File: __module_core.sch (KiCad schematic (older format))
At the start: 68 parts, among them J1 Vref, J2 bus_L, J3 tri, J4 bus_R, J5 power_bus, U1 TL074, U2 L78L05_TO92, U3 L79L05_TO92, U4 SSI2131, U5 LM317L_TO92

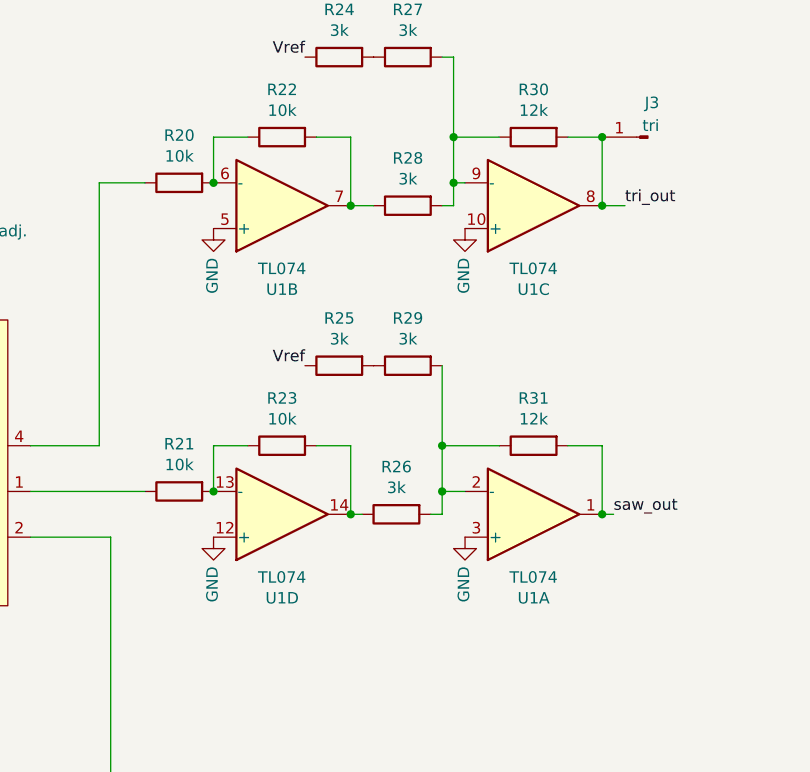
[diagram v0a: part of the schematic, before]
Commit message: Artworks on pcbs are done.
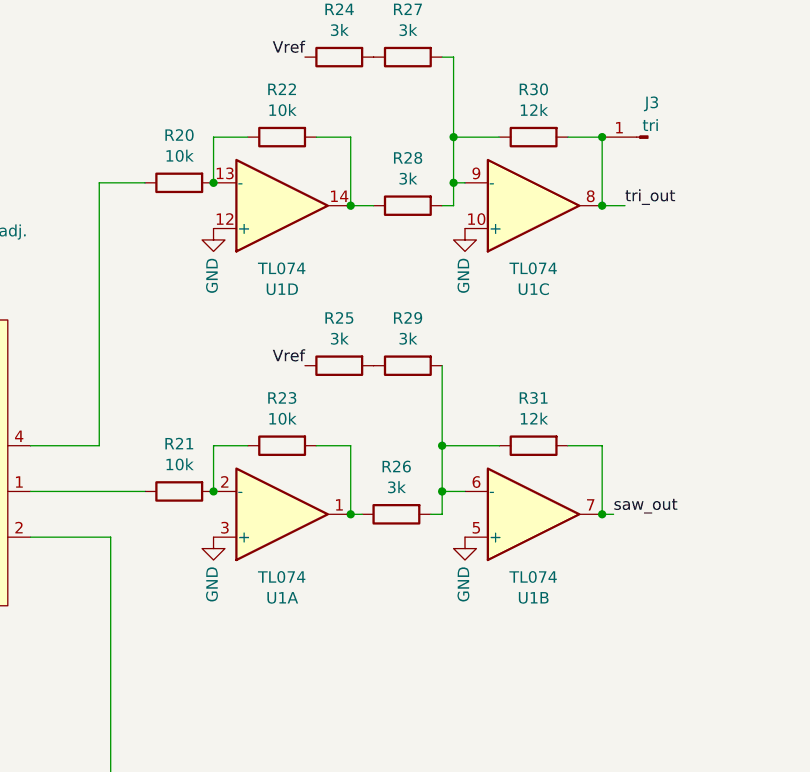
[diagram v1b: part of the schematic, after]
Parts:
- C14, C16, C18: footprint Capacitor_THT:CP_Radial_D5.0mm_P2.50mm -> Capacitor_THT:CP_Radial_Tantal_D5.0mm_P2.50mm
- C7: footprint Capacitor_THT:C_Radial_D10.0mm_H12.5mm_P5.00mm -> Attenuverter:C_Axial_L4.8mm_D3.1mm_P5.08mm_Horizontal
- D3: footprint Diode_THT:D_DO-35_SOD27_P7.62mm_Horizontal -> Diode_THT:D_DO-35_SOD27_P2.54mm_Vertical_AnodeUp
- U2, U3, U5: footprint Package_TO_SOT_THT:TO-92_Inline -> Package_TO_SOT_THT:TO-92_Inline_Wide
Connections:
- net saw_out: now also U1.7; no longer U1.1
- net at R20.2, R22.1: now also U1.13 (-); no longer U1.6 (-)
- net at R22.2, R28.1: now also U1.14; no longer U1.7
- net at R21.2, R23.1: now also U1.2 (-); no longer U1.13 (-)
- net at R23.2, R26.1: now also U1.1; no longer U1.14
- net at R26.2, R29.2, R31.1: now also U1.6 (-); no longer U1.2 (-)
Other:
- moved on the sheet: U1A, U1B, U1D
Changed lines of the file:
@@
 $Descr A4 11693 8268
 encoding utf-8
-Sheet 2 3
+Sheet 2 2
 Title ""
 Date ""
@@
 F 0 "C7" V 4102 1450 50  0000 C CNN
 F 1 "1u" V 4011 1450 50  0000 C CNN
-F 2 "Capacitor_THT:C_Radial_D10.0mm_H12.5mm_P5.00mm" H 3888 1300 50  0001 C CNN
+F 2 "Attenuverter:C_Axial_L4.8mm_D3.1mm_P5.08mm_Horizontal" H 3888 1300 50  0001 C CNN
 F 3 "~" H 3850 1450 50  0001 C CNN
 	1    3850 1450
@@
 F 0 "U2" H 3700 6742 50  0000 C CNN
 F 1 "L78L05_TO92" H 3700 6651 50  0000 C CNN
-F 2 "Package_TO_SOT_THT:TO-92_Inline" H 3700 6725 50  0001 C CIN
+F 2 "Package_TO_SOT_THT:TO-92_Inline_Wide" H 3700 6725 50  0001 C CIN
 F 3 "http://www.st.com/content/ccc/resource/technical/document/datasheet/15/55/e5/aa/23/5b/43/fd/CD00000446.pdf/files/CD00000446.pdf/jcr:content/translations/en.CD00000446.pdf" H 3700 6450 50  0001 C CNN
 	1    3700 6500
@@
 F 0 "U3" H 3700 6951 50  0000 C CNN
 F 1 "L79L05_TO92" H 3700 6860 50  0000 C CNN
-F 2 "Package_TO_SOT_THT:TO-92_Inline" H 3700 6900 50  0001 C CIN
+F 2 "Package_TO_SOT_THT:TO-92_Inline_Wide" H 3700 6900 50  0001 C CIN
 F 3 "http://www.farnell.com/datasheets/1827870.pdf" H 3700 7100 50  0001 C CNN
 	1    3700 7100
@@
 L Amplifier_Operational:TL074 U?
 U 2 1 6466712E
-P 7600 1500
+P 8700 2850
 AR Path="/6466712E" Ref="U?"  Part="2"
 AR Path="/64492573/6466712E" Ref="U1"  Part="2"
-F 0 "U1" H 7600 1867 50  0000 C CNN
-F 1 "TL074" H 7600 1776 50  0000 C CNN
-F 2 "Package_DIP:DIP-14_W7.62mm" H 7550 1600 50  0001 C CNN
-F 3 "http://www.ti.com/lit/ds/symlink/tl071.pdf" H 7650 1700 50  0001 C CNN
-	2    7600 1500
+F 0 "U1" H 8700 3217 50  0000 C CNN
+F 1 "TL074" H 8700 3126 50  0000 C CNN
+F 2 "Package_DIP:DIP-14_W7.62mm" H 8650 2950 50  0001 C CNN
+F 3 "http://www.ti.com/lit/ds/symlink/tl071.pdf" H 8750 3050 50  0001 C CNN
+	2    8700 2850
 	1    0    0    1
 $EndComp
@@
 L Amplifier_Operational:TL074 U?
 U 4 1 6466713A
-P 7600 2850
+P 7600 1500
 AR Path="/6466713A" Ref="U?"  Part="4"
 AR Path="/64492573/6466713A" Ref="U1"  Part="4"
-F 0 "U1" H 7600 3217 50  0000 C CNN
-F 1 "TL074" H 7600 3126 50  0000 C CNN
-F 2 "Package_DIP:DIP-14_W7.62mm" H 7550 2950 50  0001 C CNN
-F 3 "http://www.ti.com/lit/ds/symlink/tl071.pdf" H 7650 3050 50  0001 C CNN
-	4    7600 2850
+F 0 "U1" H 7600 1867 50  0000 C CNN
+F 1 "TL074" H 7600 1776 50  0000 C CNN
+F 2 "Package_DIP:DIP-14_W7.62mm" H 7550 1600 50  0001 C CNN
+F 3 "http://www.ti.com/lit/ds/symlink/tl071.pdf" H 7650 1700 50  0001 C CNN
+	4    7600 1500
 	1    0    0    1
 $EndComp
@@
 L Amplifier_Operational:TL074 U?
 U 1 1 64667205
-P 8700 2850
+P 7600 2850
 AR Path="/64667205" Ref="U?"  Part="1"
 AR Path="/64492573/64667205" Ref="U1"  Part="1"
-F 0 "U1" H 8700 3217 50  0000 C CNN
-F 1 "TL074" H 8700 3126 50  0000 C CNN
-F 2 "Package_DIP:DIP-14_W7.62mm" H 8650 2950 50  0001 C CNN
-F 3 "http://www.ti.com/lit/ds/symlink/tl071.pdf" H 8750 3050 50  0001 C CNN
-	1    8700 2850
+F 0 "U1" H 7600 3217 50  0000 C CNN
+F 1 "TL074" H 7600 3126 50  0000 C CNN
+F 2 "Package_DIP:DIP-14_W7.62mm" H 7550 2950 50  0001 C CNN
+F 3 "http://www.ti.com/lit/ds/symlink/tl071.pdf" H 7650 3050 50  0001 C CNN
+	1    7600 2850
 	1    0    0    1
 $EndComp
@@
 F 0 "U5" H 5800 6442 50  0000 C CNN
 F 1 "LM317L_TO92" H 5800 6351 50  0000 C CNN
-F 2 "Package_TO_SOT_THT:TO-92_Inline" H 5800 6425 50  0001 C CIN
+F 2 "Package_TO_SOT_THT:TO-92_Inline_Wide" H 5800 6425 50  0001 C CIN
 F 3 "http://www.ti.com/lit/ds/snvs775k/snvs775k.pdf" H 5800 6200 50  0001 C CNN
 	1    5800 6200
@@
 F 0 "C16" H 5918 6996 50  0000 L CNN
 F 1 "10u" H 5918 6905 50  0000 L CNN
-F 2 "Capacitor_THT:CP_Radial_D5.0mm_P2.50mm" H 5838 6800 50  0001 C CNN
+F 2 "Capacitor_THT:CP_Radial_Tantal_D5.0mm_P2.50mm" H 5838 6800 50  0001 C CNN
 F 3 "~" H 5800 6950 50  0001 C CNN
 	1    5800 6950
@@
 F 0 "D3" H 5800 6067 50  0000 C CNN
 F 1 "1N4148" H 5800 5976 50  0000 C CNN
-F 2 "Diode_THT:D_DO-35_SOD27_P7.62mm_Horizontal" H 5800 5675 50  0001 C CNN
+F 2 "Diode_THT:D_DO-35_SOD27_P2.54mm_Vertical_AnodeUp" H 5800 5675 50  0001 C CNN
 F 3 "https://assets.nexperia.com/documents/data-sheet/1N4148_1N4448.pdf" H 5800 5850 50  0001 C CNN
 	1    5800 5850
@@
 F 0 "C14" H 5418 6396 50  0000 L CNN
 F 1 "1u" H 5418 6305 50  0000 L CNN
-F 2 "Capacitor_THT:CP_Radial_D5.0mm_P2.50mm" H 5338 6200 50  0001 C CNN
+F 2 "Capacitor_THT:CP_Radial_Tantal_D5.0mm_P2.50mm" H 5338 6200 50  0001 C CNN
 F 3 "~" H 5300 6350 50  0001 C CNN
 	1    5300 6350
@@
 F 0 "C18" H 6818 6396 50  0000 L CNN
 F 1 "1u" H 6818 6305 50  0000 L CNN
-F 2 "Capacitor_THT:CP_Radial_D5.0mm_P2.50mm" H 6738 6200 50  0001 C CNN
+F 2 "Capacitor_THT:CP_Radial_Tantal_D5.0mm_P2.50mm" H 6738 6200 50  0001 C CNN
 F 3 "~" H 6700 6350 50  0001 C CNN
 	1    6700 6350
